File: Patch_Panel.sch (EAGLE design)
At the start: 34 parts

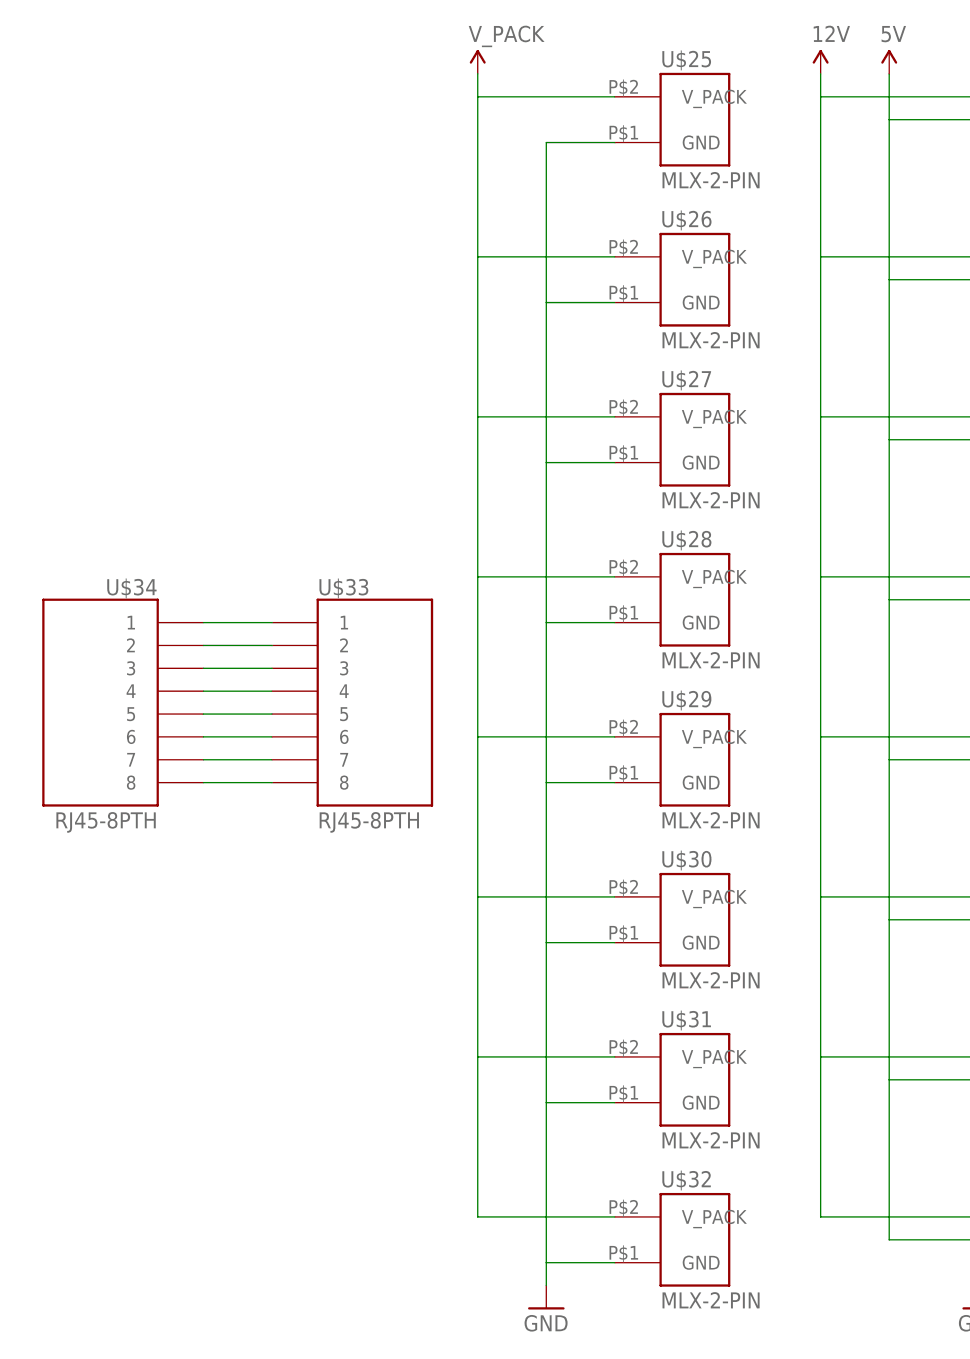
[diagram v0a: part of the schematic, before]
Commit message: Removed 2-pin Connectors and RJ45 Pass-Through
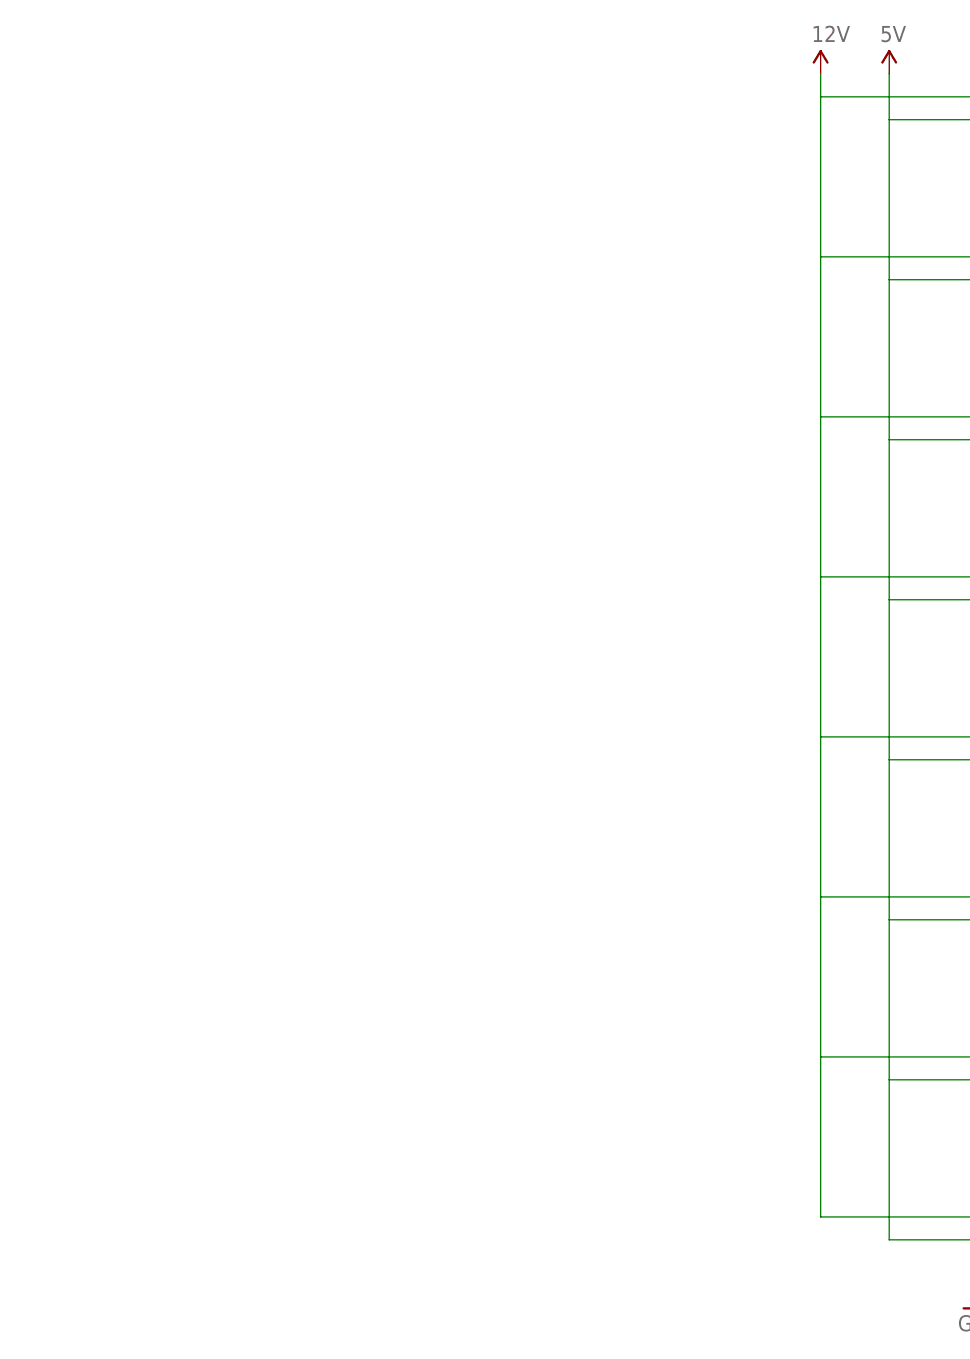
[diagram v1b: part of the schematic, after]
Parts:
- removed U$25, U$26, U$27, U$28, U$29, U$30, U$31, U$32: MLX-2-PIN, MRDT-2015-General:MLX-2-PIN
- removed U$33, U$34: RJ45-8PTH, SparkFun-Connectors:RJ45-8PTH
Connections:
- removed net N$1: U$33.1, U$34.1
- removed net N$2: U$33.2, U$34.2
- removed net N$3: U$33.3, U$34.3
- removed net N$4: U$33.4, U$34.4
- removed net N$5: U$33.5, U$34.5
- removed net N$6: U$33.6, U$34.6
- removed net N$7: U$33.7, U$34.7
- removed net N$8: U$33.8, U$34.8
- net 12V: no longer U$25.V_PACK, U$26.V_PACK, U$27.V_PACK, U$28.V_PACK, U$29.V_PACK, U$30.V_PACK, U$31.V_PACK, U$32.V_PACK
- net GND: no longer U$25.GND, U$26.GND, U$27.GND, U$28.GND, U$29.GND, U$30.GND, U$31.GND, U$32.GND
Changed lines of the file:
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@@
 <?xml version="1.0" encoding="utf-8"?>
 <!DOCTYPE eagle SYSTEM "eagle.dtd">
-<eagle version="6.5.0">
+<eagle version="7.3.0">
 <drawing>
 <settings>
@@
 <part name="SUPPLY6" library="SparkFun-Aesthetics" deviceset="12V" device=""/>
 <part name="GND3" library="SparkFun-Aesthetics" deviceset="GND" device=""/>
-<part name="U$25" library="MRDT-2015-General" deviceset="MLX-2-PIN" device=""/>
-<part name="U$26" library="MRDT-2015-General" deviceset="MLX-2-PIN" device=""/>
-<part name="U$27" library="MRDT-2015-General" deviceset="MLX-2-PIN" device=""/>
-<part name="U$28" library="MRDT-2015-General" deviceset="MLX-2-PIN" device=""/>
-<part name="U$29" library="MRDT-2015-General" deviceset="MLX-2-PIN" device=""/>
-<part name="U$30" library="MRDT-2015-General" deviceset="MLX-2-PIN" device=""/>
-<part name="U$31" library="MRDT-2015-General" deviceset="MLX-2-PIN" device=""/>
-<part name="U$32" library="MRDT-2015-General" deviceset="MLX-2-PIN" device=""/>
-<part name="V_PACK" library="SparkFun-Aesthetics" deviceset="12V" device="" value="V_PACK"/>
-<part name="GND4" library="SparkFun-Aesthetics" deviceset="GND" device=""/>
-<part name="U$33" library="SparkFun-Connectors" deviceset="RJ45-8" device="PTH"/>
-<part name="U$34" library="SparkFun-Connectors" deviceset="RJ45-8" device="PTH"/>
 </parts>
 <sheets>
@@
 <instance part="SUPPLY6" gate="G$1" x="33.02" y="149.86"/>
 <instance part="GND3" gate="1" x="50.8" y="12.7"/>
-<instance part="U$25" gate="G$1" x="-68.58" y="144.78"/>
-<instance part="U$26" gate="G$1" x="-68.58" y="127"/>
-<instance part="U$27" gate="G$1" x="-68.58" y="109.22"/>
-<instance part="U$28" gate="G$1" x="-68.58" y="91.44"/>
-<instance part="U$29" gate="G$1" x="-68.58" y="73.66"/>
-<instance part="U$30" gate="G$1" x="-68.58" y="55.88"/>
-<instance part="U$31" gate="G$1" x="-68.58" y="38.1"/>
-<instance part="U$32" gate="G$1" x="-68.58" y="20.32"/>
-<instance part="V_PACK" gate="G$1" x="-91.44" y="149.86"/>
-<instance part="GND4" gate="1" x="-83.82" y="12.7"/>
-<instance part="U$33" gate="G$1" x="-101.6" y="78.74"/>
-<instance part="U$34" gate="G$1" x="-134.62" y="78.74" rot="MR0"/>
 </instances>
 <busses>
@@
 <wire x1="55.88" y1="40.64" x2="33.02" y2="40.64" width="0.1524" layer="91"/>
 </segment>
-<segment>
-<pinref part="U$32" gate="G$1" pin="V_PACK"/>
-<pinref part="V_PACK" gate="G$1" pin="12V"/>
-<wire x1="-76.2" y1="22.86" x2="-91.44" y2="22.86" width="0.1524" layer="91"/>
-<wire x1="-91.44" y1="22.86" x2="-91.44" y2="40.64" width="0.1524" layer="91"/>
-<pinref part="U$25" gate="G$1" pin="V_PACK"/>
-<wire x1="-91.44" y1="40.64" x2="-91.44" y2="58.42" width="0.1524" layer="91"/>
-<wire x1="-91.44" y1="58.42" x2="-91.44" y2="76.2" width="0.1524" layer="91"/>
-<wire x1="-91.44" y1="76.2" x2="-91.44" y2="93.98" width="0.1524" layer="91"/>
-<wire x1="-91.44" y1="93.98" x2="-91.44" y2="111.76" width="0.1524" layer="91"/>
-<wire x1="-91.44" y1="111.76" x2="-91.44" y2="129.54" width="0.1524" layer="91"/>
-<wire x1="-91.44" y1="129.54" x2="-91.44" y2="147.32" width="0.1524" layer="91"/>
-<wire x1="-91.44" y1="147.32" x2="-91.44" y2="149.86" width="0.1524" layer="91"/>
-<wire x1="-76.2" y1="147.32" x2="-91.44" y2="147.32" width="0.1524" layer="91"/>
-<pinref part="U$26" gate="G$1" pin="V_PACK"/>
-<wire x1="-76.2" y1="129.54" x2="-91.44" y2="129.54" width="0.1524" layer="91"/>
-<pinref part="U$27" gate="G$1" pin="V_PACK"/>
-<wire x1="-76.2" y1="111.76" x2="-91.44" y2="111.76" width="0.1524" layer="91"/>
-<pinref part="U$28" gate="G$1" pin="V_PACK"/>
-<wire x1="-76.2" y1="93.98" x2="-91.44" y2="93.98" width="0.1524" layer="91"/>
-<pinref part="U$29" gate="G$1" pin="V_PACK"/>
-<wire x1="-76.2" y1="76.2" x2="-91.44" y2="76.2" width="0.1524" layer="91"/>
-<pinref part="U$30" gate="G$1" pin="V_PACK"/>
-<wire x1="-76.2" y1="58.42" x2="-91.44" y2="58.42" width="0.1524" layer="91"/>
-<pinref part="U$31" gate="G$1" pin="V_PACK"/>
-<wire x1="-76.2" y1="40.64" x2="-91.44" y2="40.64" width="0.1524" layer="91"/>
-</segment>
 </net>
 <net name="GND" class="0">
@@
 <wire x1="55.88" y1="17.78" x2="50.8" y2="17.78" width="0.1524" layer="91"/>
 </segment>
-<segment>
-<pinref part="U$25" gate="G$1" pin="GND"/>
-<pinref part="GND4" gate="1" pin="GND"/>
-<wire x1="-76.2" y1="142.24" x2="-83.82" y2="142.24" width="0.1524" layer="91"/>
-<wire x1="-83.82" y1="142.24" x2="-83.82" y2="124.46" width="0.1524" layer="91"/>
-<pinref part="U$26" gate="G$1" pin="GND"/>
-<wire x1="-83.82" y1="124.46" x2="-83.82" y2="106.68" width="0.1524" layer="91"/>
-<wire x1="-83.82" y1="106.68" x2="-83.82" y2="88.9" width="0.1524" layer="91"/>
-<wire x1="-83.82" y1="88.9" x2="-83.82" y2="71.12" width="0.1524" layer="91"/>
-<wire x1="-83.82" y1="71.12" x2="-83.82" y2="53.34" width="0.1524" layer="91"/>
-<wire x1="-83.82" y1="53.34" x2="-83.82" y2="35.56" width="0.1524" layer="91"/>
-<wire x1="-83.82" y1="35.56" x2="-83.82" y2="17.78" width="0.1524" layer="91"/>
-<wire x1="-83.82" y1="17.78" x2="-83.82" y2="15.24" width="0.1524" layer="91"/>
-<wire x1="-76.2" y1="124.46" x2="-83.82" y2="124.46" width="0.1524" layer="91"/>
-<pinref part="U$27" gate="G$1" pin="GND"/>
-<wire x1="-76.2" y1="106.68" x2="-83.82" y2="106.68" width="0.1524" layer="91"/>
-<pinref part="U$28" gate="G$1" pin="GND"/>
-<wire x1="-76.2" y1="88.9" x2="-83.82" y2="88.9" width="0.1524" layer="91"/>
-<pinref part="U$29" gate="G$1" pin="GND"/>
-<wire x1="-76.2" y1="71.12" x2="-83.82" y2="71.12" width="0.1524" layer="91"/>
-<pinref part="U$30" gate="G$1" pin="GND"/>
-<wire x1="-76.2" y1="53.34" x2="-83.82" y2="53.34" width="0.1524" layer="91"/>
-<pinref part="U$31" gate="G$1" pin="GND"/>
-<wire x1="-76.2" y1="35.56" x2="-83.82" y2="35.56" width="0.1524" layer="91"/>
-<pinref part="U$32" gate="G$1" pin="GND"/>
-<wire x1="-76.2" y1="17.78" x2="-83.82" y2="17.78" width="0.1524" layer="91"/>
-</segment>
 </net>
-<net name="N$1" class="0">
-<segment>
-<pinref part="U$34" gate="G$1" pin="1"/>
-<pinref part="U$33" gate="G$1" pin="1"/>
-<wire x1="-121.92" y1="88.9" x2="-114.3" y2="88.9" width="0.1524" layer="91"/>
-</segment>
-</net>
-<net name="N$2" class="0">
-<segment>
-<pinref part="U$34" gate="G$1" pin="2"/>
-<pinref part="U$33" gate="G$1" pin="2"/>
-<wire x1="-121.92" y1="86.36" x2="-114.3" y2="86.36" width="0.1524" layer="91"/>
-</segment>
-</net>
-<net name="N$3" class="0">
-<segment>
-<pinref part="U$34" gate="G$1" pin="3"/>
-<pinref part="U$33" gate="G$1" pin="3"/>
-<wire x1="-121.92" y1="83.82" x2="-114.3" y2="83.82" width="0.1524" layer="91"/>
-</segment>
-</net>
-<net name="N$4" class="0">
-<segment>
-<pinref part="U$34" gate="G$1" pin="4"/>
-<pinref part="U$33" gate="G$1" pin="4"/>
-<wire x1="-121.92" y1="81.28" x2="-114.3" y2="81.28" width="0.1524" layer="91"/>
-</segment>
-</net>
-<net name="N$5" class="0">
-<segment>
-<pinref part="U$34" gate="G$1" pin="5"/>
-<pinref part="U$33" gate="G$1" pin="5"/>
-<wire x1="-121.92" y1="78.74" x2="-114.3" y2="78.74" width="0.1524" layer="91"/>
-</segment>
-</net>
-<net name="N$6" class="0">
-<segment>
-<pinref part="U$34" gate="G$1" pin="6"/>
-<pinref part="U$33" gate="G$1" pin="6"/>
-<wire x1="-121.92" y1="76.2" x2="-114.3" y2="76.2" width="0.1524" layer="91"/>
-</segment>
-</net>
-<net name="N$7" class="0">
-<segment>
-<pinref part="U$34" gate="G$1" pin="7"/>
-<pinref part="U$33" gate="G$1" pin="7"/>
-<wire x1="-121.92" y1="73.66" x2="-114.3" y2="73.66" width="0.1524" layer="91"/>
-</segment>
-</net>
-<net name="N$8" class="0">
-<segment>
-<pinref part="U$34" gate="G$1" pin="8"/>
-<pinref part="U$33" gate="G$1" pin="8"/>
-<wire x1="-121.92" y1="71.12" x2="-114.3" y2="71.12" width="0.1524" layer="91"/>
-</segment>
-</net>
